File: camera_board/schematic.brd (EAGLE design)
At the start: 100 x 80 mm, 7 parts

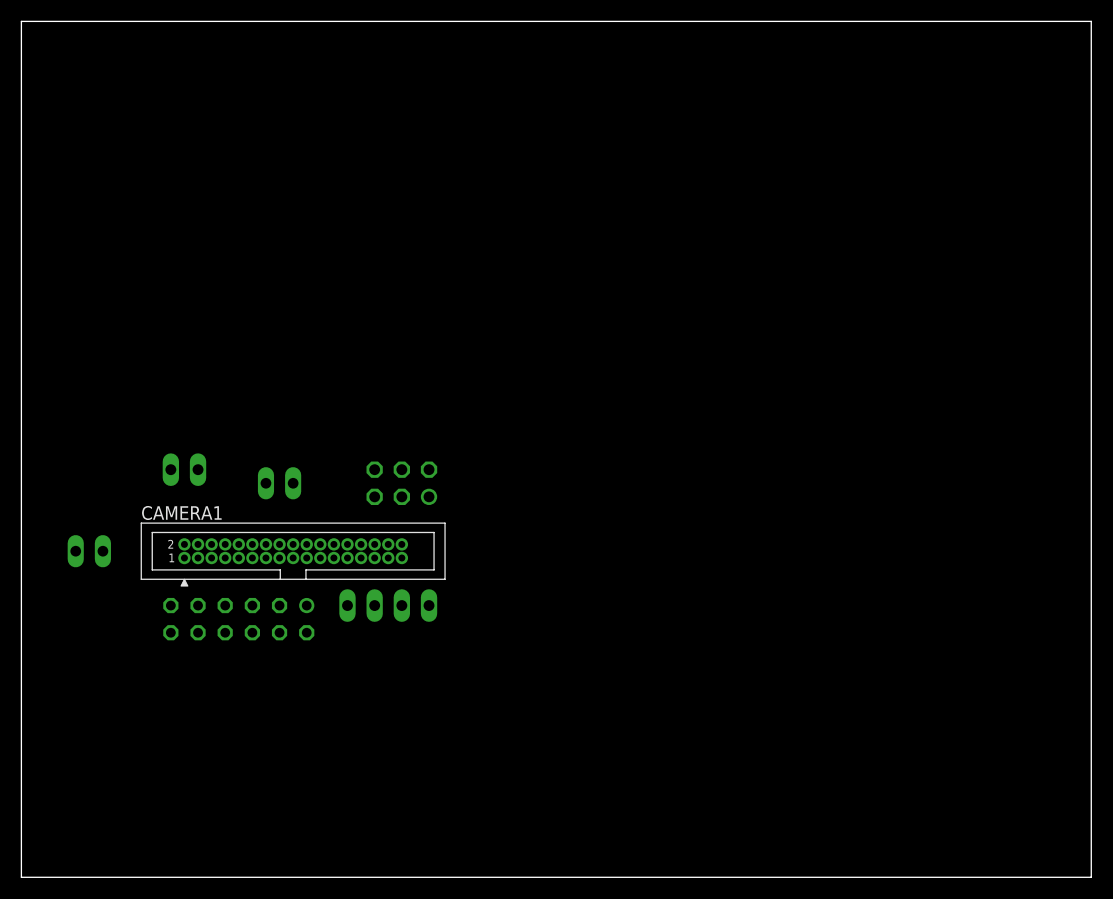
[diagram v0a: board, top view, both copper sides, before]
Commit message: Updated Schematic and Board
I'm debating on removing the ccd_data pin breakout all together - more
to come on this
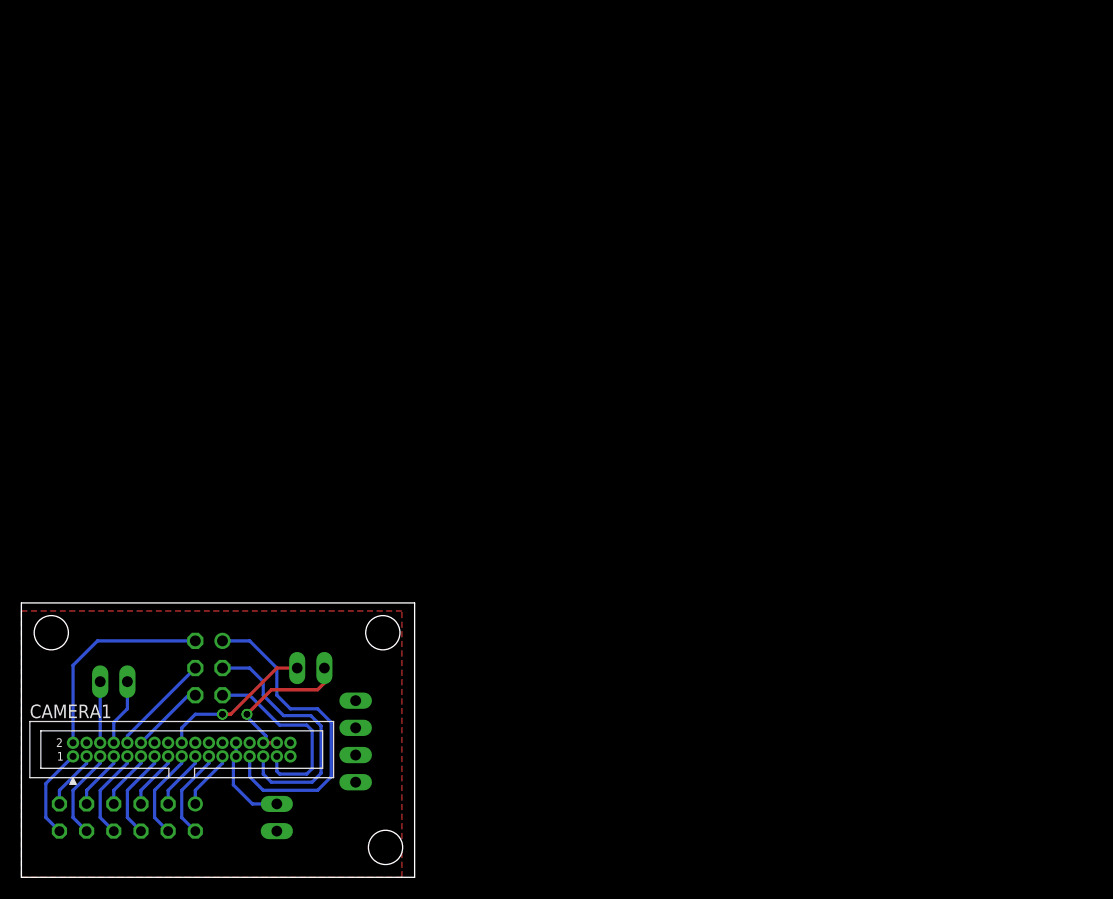
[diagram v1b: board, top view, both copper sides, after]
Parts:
- moved POWER1 30.4 mm to (23.9, 5.59), turned to 90 degrees
- moved CONTROL 25.0 mm to (17.5, 19.6), turned to 270 degrees
- moved CAMERA1 21.3 mm to (15.0, 11.9)
- moved DATA 21.3 mm to (9.91, 5.59)
- moved SERIAL 20.9 mm to (8.64, 18.3)
- moved PWR2 17.5 mm to (27.1, 19.6)
- moved CCD_DATA 13.1 mm to (31.2, 12.7), turned to 90 degrees
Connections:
- net N$13: now also CONTROL.6; no longer CONTROL.2
- net N$15: now also CONTROL.2; no longer CONTROL.6
- net N$16: now also CONTROL.5; no longer CONTROL.1
- net N$18: now also CONTROL.1; no longer CONTROL.5
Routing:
- net N$18: track 0.00 -> 30.5 mm
- net N$17: track 0.00 -> 24.3 mm
- net N$15: track 0.00 -> 19.6 mm
- net N$16: track 0.00 -> 18.3 mm
- net 1.8V: track 0.00 -> 14.6 mm, vias 0 -> 1
- net 2.8V: track 0.00 -> 14.5 mm, vias 0 -> 1
- net N$14: track 0.00 -> 9.62 mm
- net VCC: track 0.00 -> 8.84 mm
- net N$8: track 0.00 -> 8.56 mm
- net N$4: track 0.00 -> 8.56 mm
- net N$10: track 0.00 -> 8.56 mm
- net N$6: track 0.00 -> 8.56 mm
- net N$2: track 0.00 -> 8.56 mm
- net N$12: track 0.00 -> 8.56 mm
- net N$13: track 0.00 -> 6.92 mm
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- added copper zone on layer 1, net GND
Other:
- board size 100 x 80 mm -> 36.8 x 25.6 mm

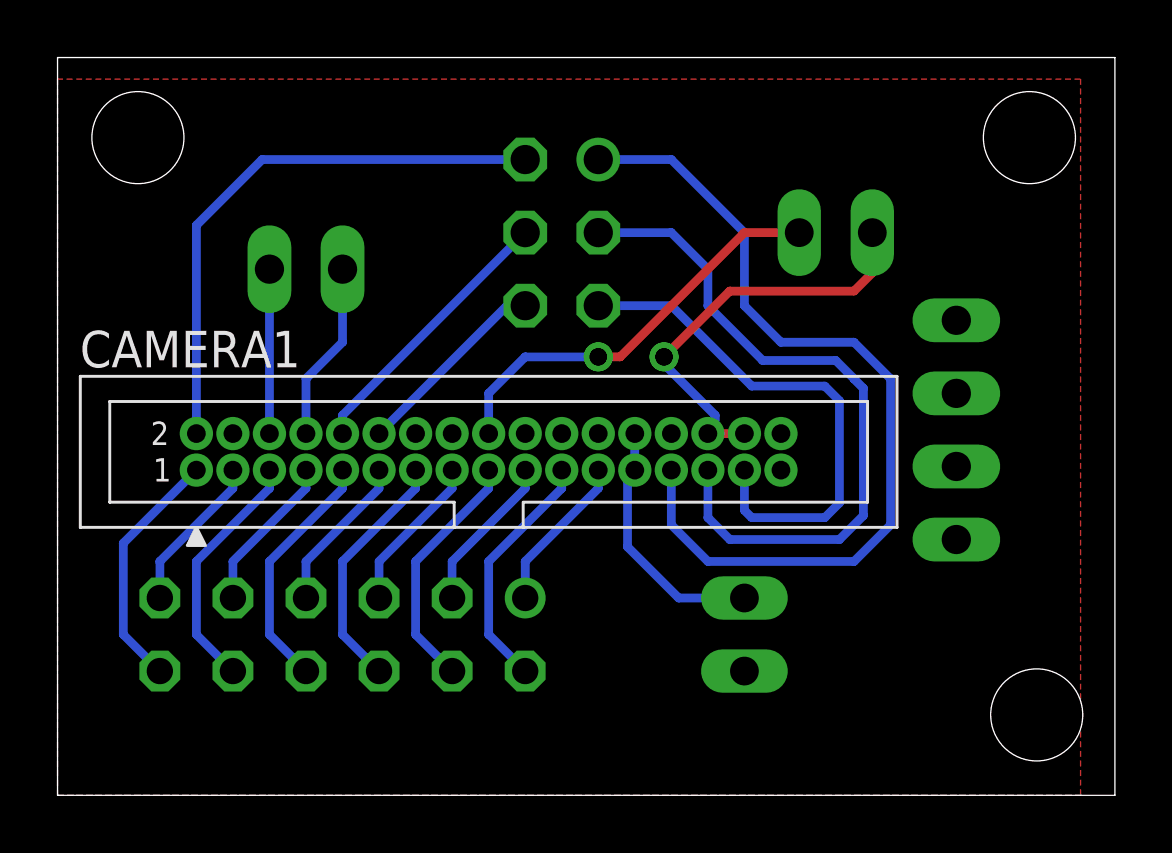
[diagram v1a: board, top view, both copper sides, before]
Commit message: Final Schematic
- Removed CCD_DATA lines, we can bodge these 4 pins if we end up needing
them but they don't appear connected in the LI-VM34LP schematic.

- Finished overall board design, added some extra text and moved around
labels so that everything comes out looking good
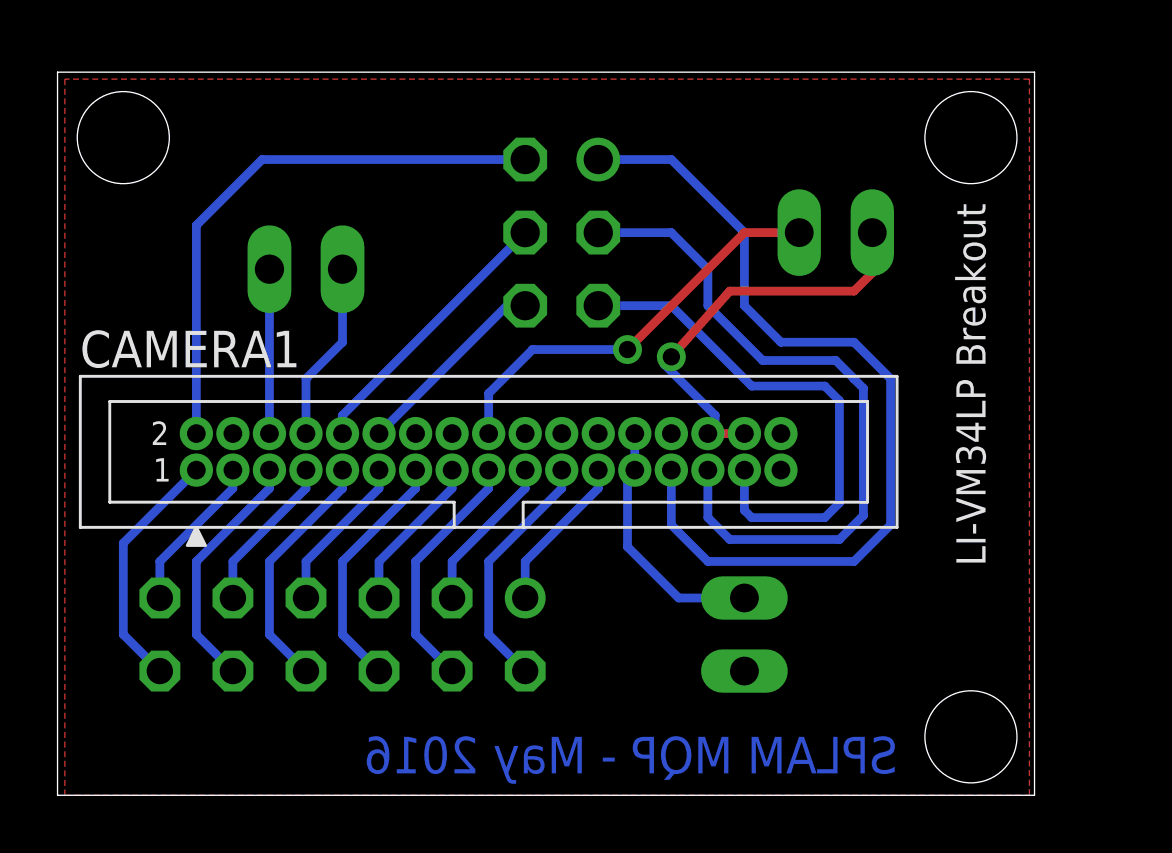
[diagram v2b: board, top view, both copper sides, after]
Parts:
- removed CCD_DATA: (no value), con-lstb:MA04-1
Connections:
- net N$19: no longer CCD_DATA.1
- net N$20: no longer CCD_DATA.2
- net N$21: no longer CCD_DATA.3
- net N$22: no longer CCD_DATA.4
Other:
- board size 36.8 x 25.6 mm -> 34 x 25.1 mm
- board text added: "LI-VM34LP Breakout"
- board text added: "SPLAM MQP - May 2016"
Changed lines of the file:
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@@
 <board>
 <plain>
-<wire x1="0" y1="0" x2="36.754" y2="0" width="0" layer="20"/>
-<wire x1="36.754" y1="0" x2="36.754" y2="25.644" width="0" layer="20"/>
-<wire x1="36.754" y1="25.644" x2="0" y2="25.644" width="0" layer="20"/>
-<wire x1="0" y1="25.644" x2="0" y2="0" width="0" layer="20"/>
-<hole x="2.794" y="22.86" drill="3.2"/>
-<hole x="34.036" y="2.794" drill="3.2"/>
-<hole x="33.782" y="22.86" drill="3.2"/>
+<wire x1="0" y1="0" x2="33.96" y2="0" width="0" layer="20"/>
+<wire x1="33.96" y1="0" x2="33.96" y2="25.136" width="0" layer="20"/>
+<wire x1="33.96" y1="25.136" x2="0" y2="25.136" width="0" layer="20"/>
+<wire x1="0" y1="25.136" x2="0" y2="0" width="0" layer="20"/>
+<hole x="2.286" y="22.86" drill="3.2"/>
+<hole x="31.75" y="2.032" drill="3.2"/>
+<hole x="31.75" y="22.86" drill="3.2"/>
+<text x="29.21" y="0.762" size="1.27" layer="16" rot="MR0">SPLAM MQP - May 2016</text>
+<text x="32.512" y="20.574" size="1.016" layer="26" rot="MR270">LI-VM34LP Breakout</text>
+<text x="31.242" y="20.574" size="1.016" layer="25" rot="R270">LI-VM34LP Breakout</text>
 </plain>
 <attributes>
@@
 <elements>
 <element name="CAMERA1" library="_hhn_con_pinhead_box_1mm27" package="PHB_1MM27_2X17_SNT" value="MT9V034" x="14.986" y="11.938"/>
-<element name="DATA" library="con-lsta" package="FE06-2" value="" x="9.906" y="5.588" rot="MR0">
+<element name="DATA" library="con-lsta" package="FE06-2" value="" x="9.906" y="5.588" smashed="yes" rot="MR0">
 <attribute name="MF" value="" x="9.906" y="5.588" size="1.778" layer="28" rot="MR0" display="off"/>
 <attribute name="MPN" value="" x="9.906" y="5.588" size="1.778" layer="28" rot="MR0" display="off"/>
 <attribute name="OC_NEWARK" value="unknown" x="9.906" y="5.588" size="1.778" layer="28" rot="MR0" display="off"/>
 <attribute name="OC_FARNELL" value="unknown" x="9.906" y="5.588" size="1.778" layer="28" rot="MR0" display="off"/>
+<attribute name="NAME" x="11.176" y="9.017" size="1.27" layer="26" ratio="10" rot="MR0"/>
+<attribute name="VALUE" x="17.526" y="0.889" size="1.27" layer="28" ratio="10" rot="MR0"/>
 </element>
 <element name="POWER1" library="con-molex" package="22-23-2021" value="MAIN" x="23.876" y="5.588" rot="MR90">
@@
 <attribute name="OC_FARNELL" value="1462926" x="27.051" y="19.558" size="1.778" layer="28" rot="MR180" display="off"/>
 </element>
-<element name="CONTROL" library="con-lstb" package="MA03-2" value="" x="17.526" y="19.558" rot="MR270">
+<element name="CONTROL" library="con-lstb" package="MA03-2" value="" x="17.526" y="19.558" smashed="yes" rot="MR270">
 <attribute name="MF" value="" x="17.526" y="19.558" size="1.778" layer="28" rot="MR270" display="off"/>
 <attribute name="MPN" value="" x="17.526" y="19.558" size="1.778" layer="28" rot="MR270" display="off"/>
 <attribute name="OC_NEWARK" value="unknown" x="17.526" y="19.558" size="1.778" layer="28" rot="MR270" display="off"/>
 <attribute name="OC_FARNELL" value="unknown" x="17.526" y="19.558" size="1.778" layer="28" rot="MR270" display="off"/>
+<attribute name="NAME" x="13.081" y="15.748" size="1.27" layer="26" ratio="10" rot="MR90"/>
+<attribute name="VALUE" x="21.717" y="20.828" size="1.27" layer="28" ratio="10" rot="MR270"/>
 </element>
-<element name="CCD_DATA" library="con-lstb" package="MA04-1" value="" x="31.242" y="12.7" rot="MR90">
-<attribute name="MF" value="" x="31.242" y="12.7" size="1.778" layer="28" rot="MR90" display="off"/>
-<attribute name="MPN" value="" x="31.242" y="12.7" size="1.778" layer="28" rot="MR90" display="off"/>
-<attribute name="OC_NEWARK" value="unknown" x="31.242" y="12.7" size="1.778" layer="28" rot="MR90" display="off"/>
-<attribute name="OC_FARNELL" value="unknown" x="31.242" y="12.7" size="1.778" layer="28" rot="MR90" display="off"/>
+<element name="SERIAL" library="pinhead" package="1X02" value="" x="8.636" y="18.288" smashed="yes" rot="MR180">
+<attribute name="NAME" x="5.0038" y="21.2852" size="1.27" layer="26" ratio="10" rot="MR180"/>
+<attribute name="VALUE" x="6.096" y="21.463" size="1.27" layer="28" rot="MR180"/>
 </element>
-<element name="SERIAL" library="pinhead" package="1X02" value="" x="8.636" y="18.288" rot="MR180"/>
 </elements>
 <signals>
@@
 <contactref element="POWER1" pad="1"/>
 <polygon width="0.3048" layer="1" isolate="0.4064">
-<vertex x="0" y="24.892"/>
-<vertex x="0" y="0"/>
-<vertex x="35.56" y="0"/>
-<vertex x="35.56" y="24.892"/>
+<vertex x="0.254" y="24.892"/>
+<vertex x="0.254" y="0"/>
+<vertex x="33.782" y="0"/>
+<vertex x="33.782" y="24.892"/>
 </polygon>
 </signal>
@@
 <wire x1="28.321" y1="18.161" x2="27.686" y2="17.526" width="0.3048" layer="1"/>
 <wire x1="27.686" y1="17.526" x2="23.368" y2="17.526" width="0.3048" layer="1"/>
-<wire x1="23.368" y1="17.526" x2="21.082" y2="15.24" width="0.3048" layer="1"/>
-<via x="21.082" y="15.24" extent="1-16" drill="0.6" shape="octagon"/>
-<wire x1="21.082" y1="15.24" x2="21.082" y2="14.986" width="0.3048" layer="16"/>
+<wire x1="23.368" y1="17.526" x2="21.336" y2="15.24" width="0.3048" layer="1"/>
+<via x="21.336" y="15.24" extent="1-16" drill="0.6" shape="octagon"/>
+<wire x1="21.336" y1="15.24" x2="21.082" y2="14.986" width="0.3048" layer="16"/>
 <wire x1="21.082" y1="14.986" x2="22.86" y2="13.208" width="0.3048" layer="16"/>
 <wire x1="22.86" y1="13.208" x2="22.86" y2="12.827" width="0.3048" layer="16"/>
@@
 <contactref element="PWR2" pad="1"/>
 <wire x1="14.986" y1="12.573" x2="14.986" y2="13.97" width="0.3048" layer="16"/>
-<wire x1="14.986" y1="13.97" x2="16.256" y2="15.24" width="0.3048" layer="16"/>
-<wire x1="16.256" y1="15.24" x2="18.796" y2="15.24" width="0.3048" layer="16"/>
-<via x="18.796" y="15.24" extent="1-16" drill="0.6" shape="octagon"/>
-<wire x1="18.796" y1="15.24" x2="19.558" y2="15.24" width="0.3048" layer="1"/>
-<wire x1="19.558" y1="15.24" x2="23.876" y2="19.558" width="0.3048" layer="1"/>
+<wire x1="14.986" y1="13.97" x2="16.51" y2="15.494" width="0.3048" layer="16"/>
+<wire x1="16.51" y1="15.494" x2="19.812" y2="15.494" width="0.3048" layer="16"/>
+<via x="19.812" y="15.494" extent="1-16" drill="0.6" shape="octagon"/>
+<wire x1="19.812" y1="15.494" x2="23.876" y2="19.558" width="0.3048" layer="1"/>
 <wire x1="23.876" y1="19.558" x2="25.781" y2="19.558" width="0.3048" layer="1"/>
 </signal>
@@
 <signal name="N$19">
 <contactref element="CAMERA1" pad="33"/>
-<contactref element="CCD_DATA" pad="1"/>
-<wire x1="25.146" y1="11.303" x2="31.242" y2="8.89" width="0" layer="19" extent="1-1"/>
 </signal>
 <signal name="N$20">
-<contactref element="CCD_DATA" pad="2"/>
 <contactref element="CAMERA1" pad="34"/>
-<wire x1="25.146" y1="12.573" x2="31.242" y2="11.43" width="0" layer="19" extent="1-1"/>
 </signal>
 <signal name="N$21">
 <contactref element="CAMERA1" pad="16"/>
-<contactref element="CCD_DATA" pad="3"/>
-<wire x1="13.716" y1="12.573" x2="31.242" y2="13.97" width="0" layer="19" extent="1-1"/>
 </signal>
 <signal name="N$22">
 <contactref element="CAMERA1" pad="24"/>
-<contactref element="CCD_DATA" pad="4"/>
-<wire x1="18.796" y1="12.573" x2="31.242" y2="16.51" width="0" layer="19" extent="1-1"/>
 </signal>
 <signal name="N$23">
@@
 <signal name="N$26">
 </signal>
-<signal name="N$25">
-<via x="18.796" y="15.24" extent="1-16" drill="0.6" shape="octagon"/>
-</signal>
-<signal name="N$27">
-<via x="21.082" y="15.24" extent="1-16" drill="0.6" shape="octagon"/>
-</signal>
 </signals>
